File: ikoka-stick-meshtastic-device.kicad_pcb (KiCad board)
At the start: 2 copper layers, 100 x 28 mm, 28 parts, among them J1 Conn_Coaxial, J2 Conn_01x07_Socket, J3 Conn_01x07_Socket, J4 Conn_01x02, J5 Conn_01x02, J6 Conn_01x04, Q1 AO3401A, SW1 SW_Push, U1 MT3608, U2 E22-900M30S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

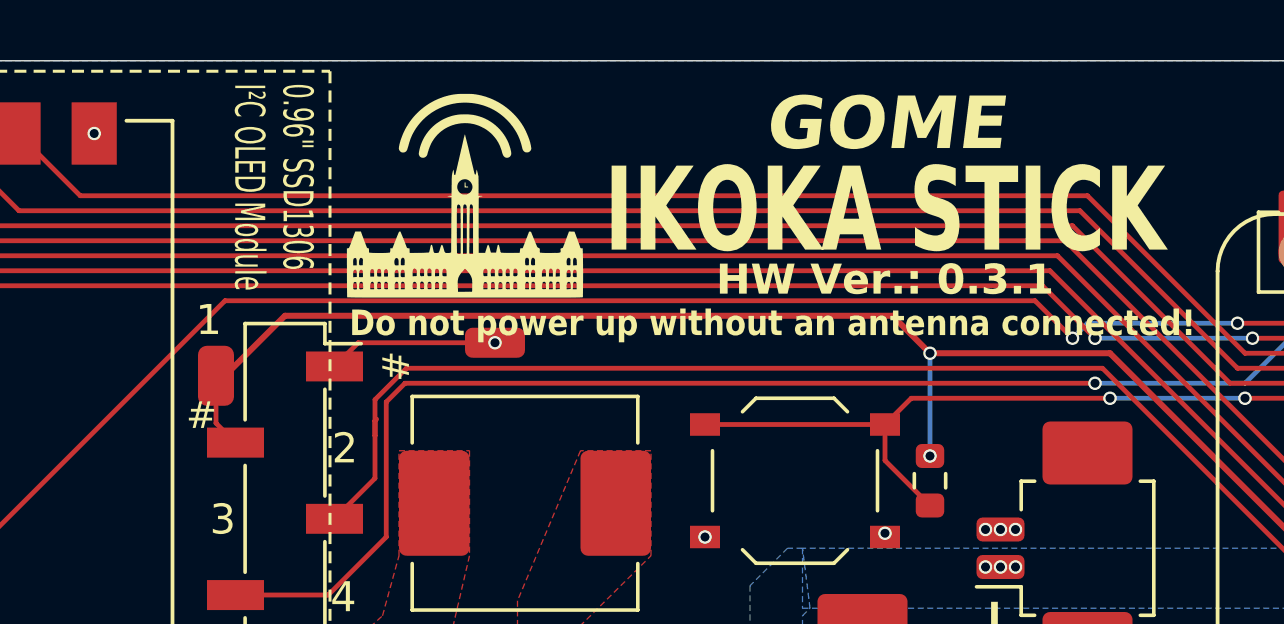
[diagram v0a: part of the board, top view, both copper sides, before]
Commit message: Baseline fixes to font, OLED header part change, exclude U3 and rotate J2,J3 properly
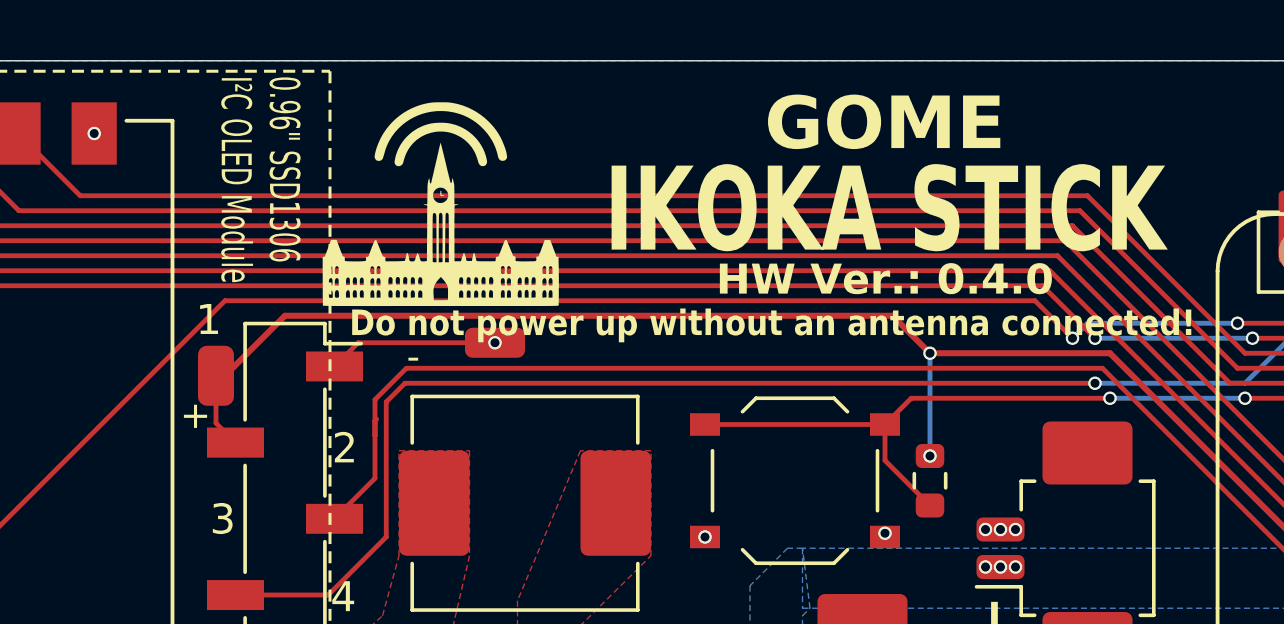
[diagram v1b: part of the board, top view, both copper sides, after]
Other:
- board text added: "HW Ver.: 0.4.0"
- board text removed: "#"
- board text removed: "HW Ver.: 0.3.1"

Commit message: use E22P, swap I2C power/gnd
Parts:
- removed REF**, pin1: SolderWirePad_1x01_SMD_1.5x3mm, Connector_Wire:SolderWirePad_1x01_SMD_1.5x3mm
- added JP1: SolderJumper_3_Bridged12, Jumper:SolderJumper-3_P1.3mm_Bridged12_RoundedPad1.0x1.5mm_NumberLabels, F.Cu at (213.7, 100.3)
- U2: value E22-900M30S -> E22P-915M30S
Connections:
- U2 pad 6: /LORA_RXEN -> Net-(JP1-C)
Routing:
- net Net-(JP1-C): track 0.00 -> 71.3 mm, vias 0 -> 2
- net /LORA_RXEN: track 67.4 -> 15.2 mm, vias 2 -> 1
- net +3V3: track 66.4 -> 75.2 mm
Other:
- board text added: "3V3"
- board text added: "E22P pin 7"
- board text added: "XIAO 6"
- board text removed: "1"
